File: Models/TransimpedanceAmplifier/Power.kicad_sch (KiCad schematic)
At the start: 0 parts

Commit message: Add tolerancing to the TIA regulator voltages
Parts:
- added U10: LM79L15, -15V, 5%, LP3_TEX, symbol LM79L:LM79L05ACZ_LFT1
- added U7: LM78L05, 5V, 5%, LP3_TEX, symbol LM78L:LM78L05ACZ_LFT1
- added U8: LM78L15, 15V, 5%, LP3_TEX, symbol LM78L:LM78L05ACZ_LFT1
- added U9: LM79L05, -5V, 5%, LP3_TEX, symbol LM79L:LM79L05ACZ_LFT1

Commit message: Save progress
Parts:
- removed U10: LM79L15, -15V, 5%, LP3_TEX, symbol LM79L:LM79L05ACZ_LFT1
- removed U7: LM78L05, 5V, 5%, LP3_TEX, symbol LM78L:LM78L05ACZ_LFT1
- removed U8: LM78L15, 15V, 5%, LP3_TEX, symbol LM78L:LM78L05ACZ_LFT1
- removed U9: LM79L05, -5V, 5%, LP3_TEX, symbol LM79L:LM79L05ACZ_LFT1
- added BT1, BT2, BT3, BT4, BT5, BT6: 9V, symbol Device:Battery
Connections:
- new net: BT4.2 (-), BT5.1 (+)
- new net: BT5.2 (-), BT6.1 (+)
- new net: BT1.2 (-), BT2.1 (+)
- new net: BT2.2 (-), BT3.1 (+)
- new net -27V: BT6.2 (-)
- new net 27V: BT1.1 (+)
- new net GND: BT3.2 (-), BT4.1 (+)
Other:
- added sheet Converter_LowVoltage (Converter_LowVoltage.kicad_sch)
- added sheet HighVoltage (HighVoltage.kicad_sch)
- added sheet PreAmp_LowVoltage (PreAmp_LowVoltage.kicad_sch)
- note added: "Negative power supply Guaranteed below -17.5 V for 0.3 A-hours"
- note added: "Positive power supply Guaranteed above 17.5 V for 0.3 A-hours 20 mA load condition ~26.9 V @ 0.0 hours ~17.5 V @ 15.0 hours 100 mA load condition ~26.6 V @ 0.0 hours ~17.5 V @ 3.0 hours"

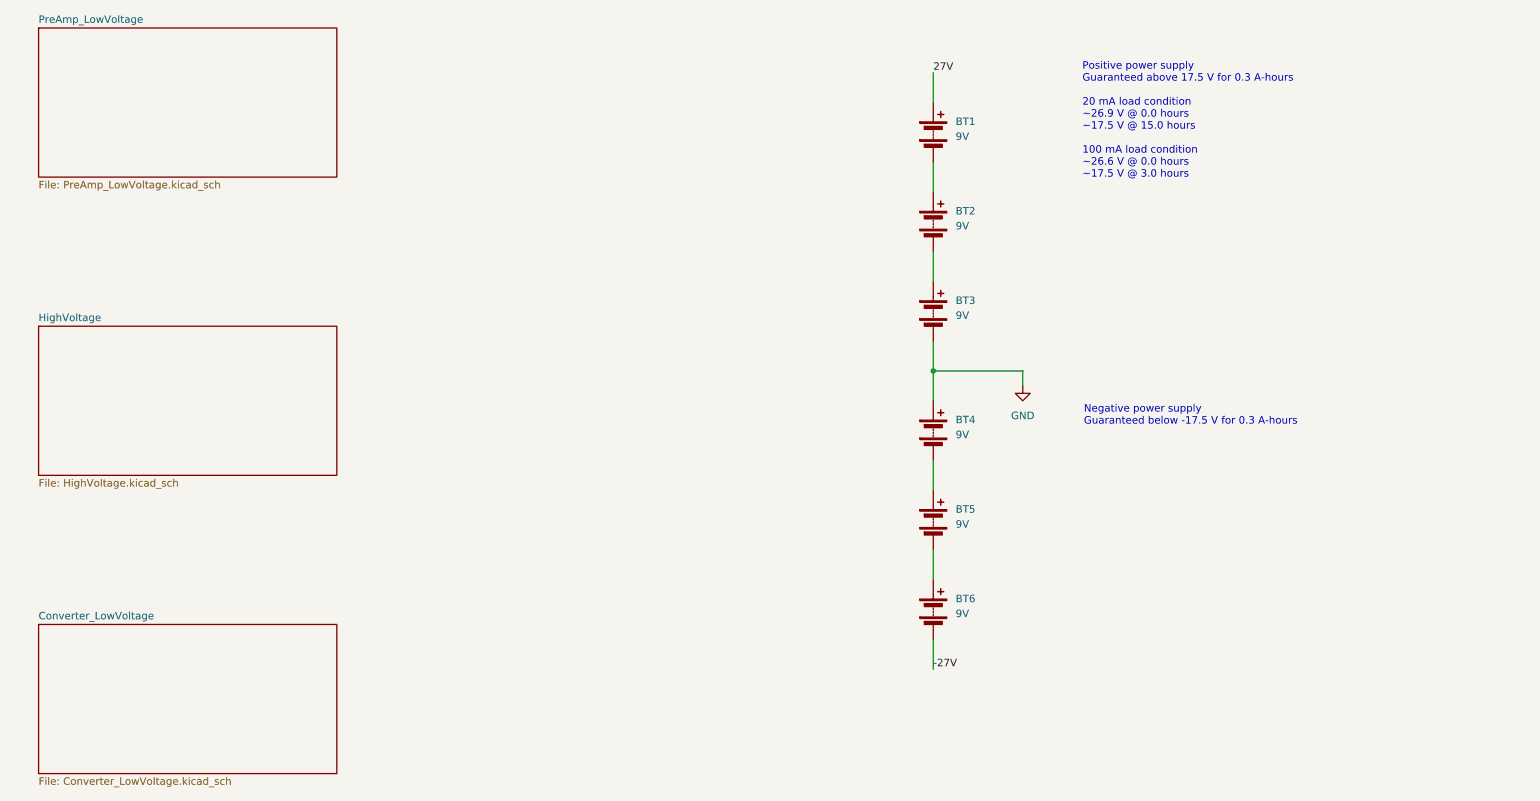
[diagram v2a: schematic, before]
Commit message: Added the 3.3V regulator choice
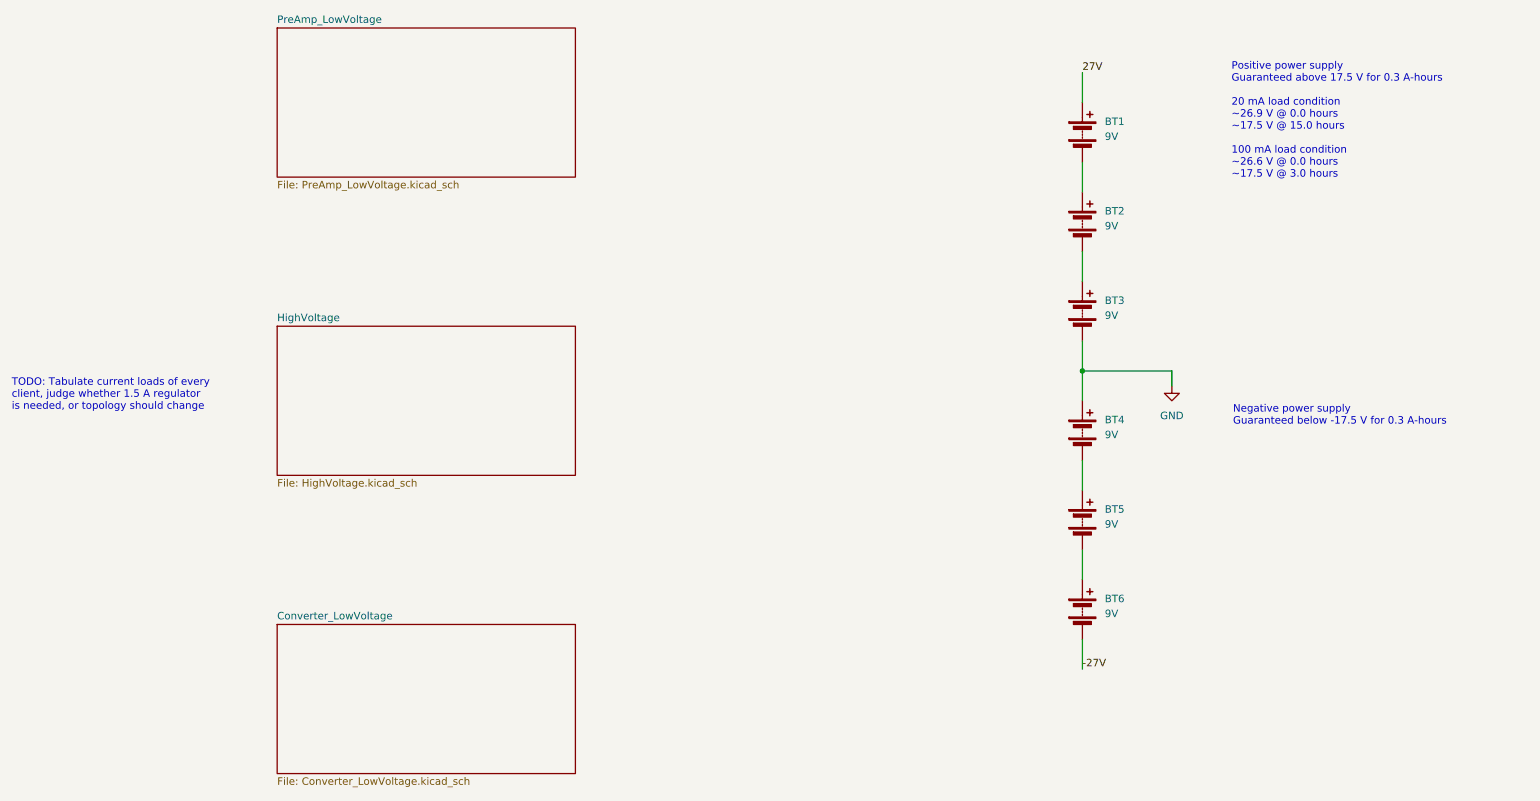
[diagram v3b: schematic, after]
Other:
- note added: "TODO: Tabulate current loads of every client, judge whether 1.5 A regulator is needed, or topology should change"
- moved on the sheet: BT1, BT2, BT3, BT4, BT5, BT6

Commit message: Labeled all the input/output nodes of the power subsystems
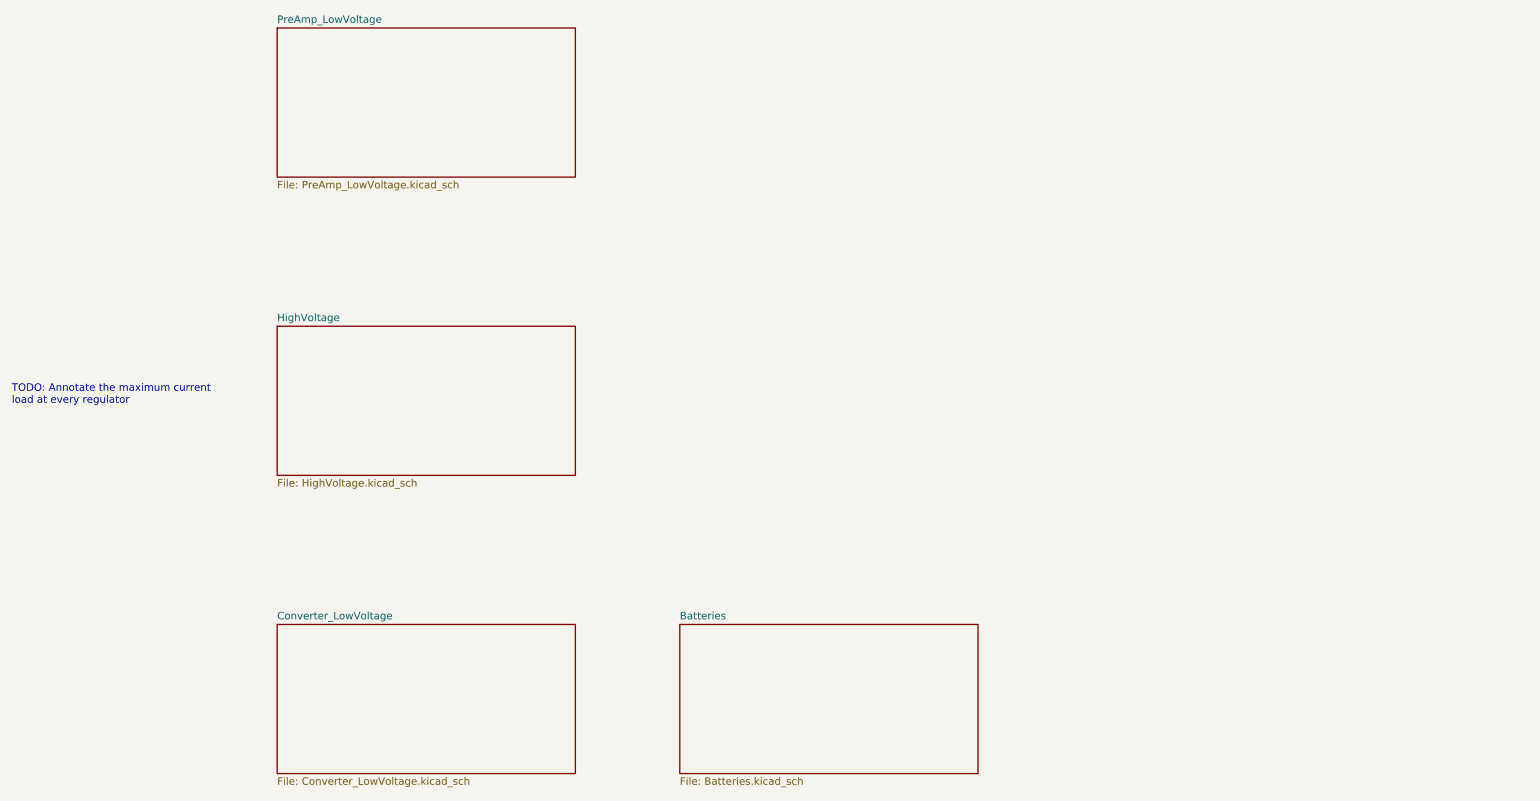
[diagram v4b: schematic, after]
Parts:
- removed BT1, BT2, BT3, BT4, BT5, BT6: 9V, symbol Device:Battery
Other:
- added sheet Batteries (Batteries.kicad_sch)
- note added: "TODO: Annotate the maximum current load at every regulator"
- note removed: "Negative power supply Guaranteed below -17.5 V for 0.3 A-hours"
- note removed: "Positive power supply Guaranteed above 17.5 V for 0.3 A-hours 20 mA load condition ~26.9 V @ 0.0 hours ~17.5 V @ 15.0 hours 100 mA load condition ~26.6 V @ 0.0 hours ~17.5 V @ 3.0 hours"
- note removed: "TODO: Tabulate current loads of every client, judge whether 1.5 A regulator is needed, or topology should change"

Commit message: Resolved the unknown regarding too much current into the 100 mA regulator
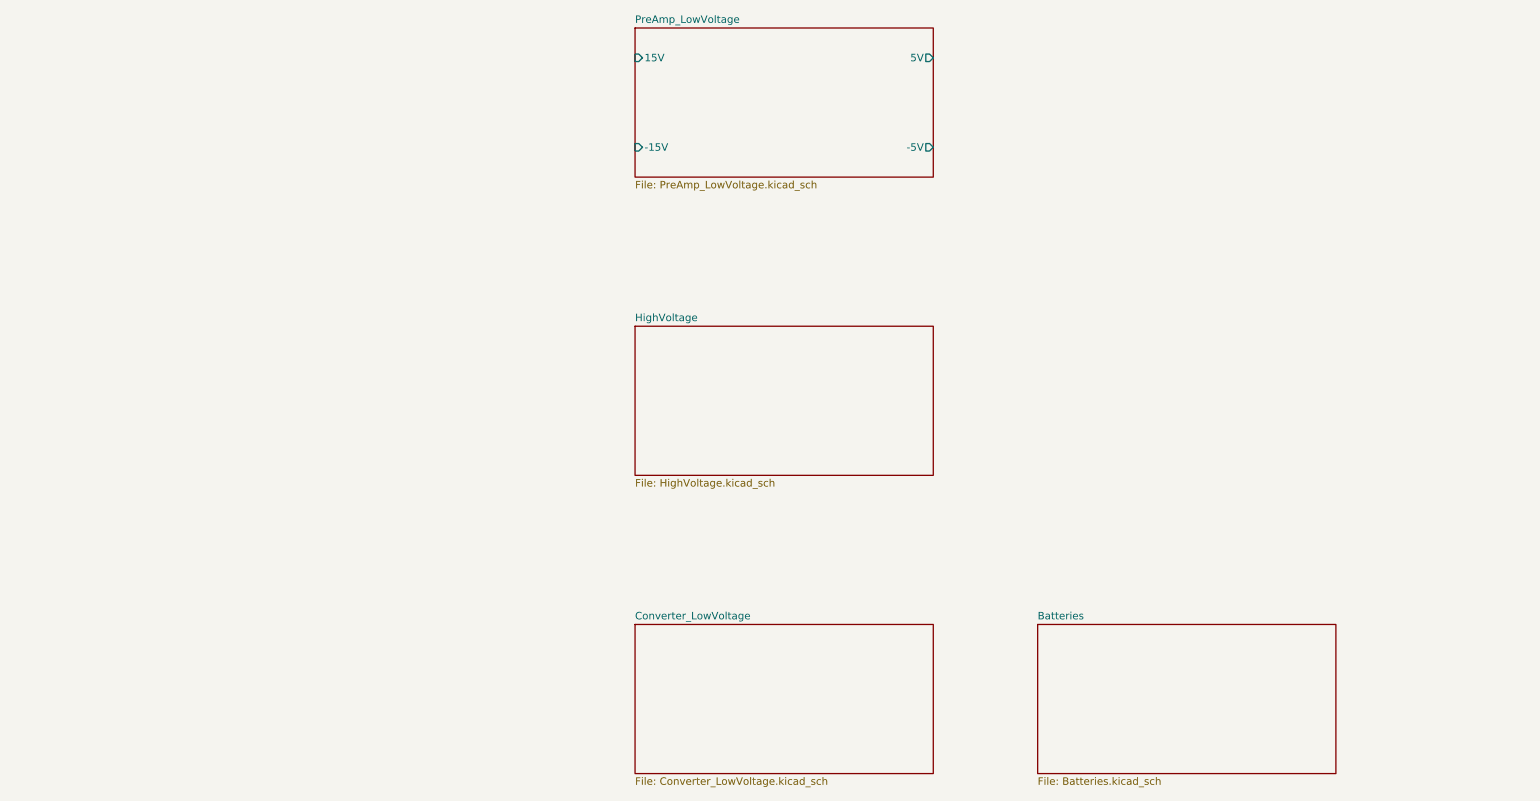
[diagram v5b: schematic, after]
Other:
- sheet PreAmp_LowVoltage ports: added -15V, -5V, 15V, 5V; removed none
- note removed: "TODO: Annotate the maximum current load at every regulator"
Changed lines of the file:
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@@
 	(generator_version "9.0")
 	(paper "A4")
-	(text "TODO: Annotate the maximum current\nload at every regulator"
-		(exclude_from_sim no)
-		(at 20.828 87.884 0)
-		(effects
-			(font
-				(size 1.27 1.27)
-			)
-			(justify left)
-		)
-	)
 	(sheet
-		(at 66.04 25.4)
+		(at 127 25.4)
 		(size 50.8 25.4)
 		(exclude_from_sim no)
@@
 		)
 		(property "Sheetname" "PreAmp_LowVoltage"
-			(at 66.04 24.6884 0)
+			(at 127 24.6884 0)
 			(effects
 				(font
@@
 		)
 		(property "Sheetfile" "PreAmp_LowVoltage.kicad_sch"
-			(at 66.04 51.3846 0)
+			(at 127 51.3846 0)
 			(effects
 				(font
@@
 				)
 				(justify left top)
+			)
+		)
+		(pin "-5V" output
+			(at 177.8 45.72 0)
+			(effects
+				(font
+					(size 1.27 1.27)
+				)
+				(justify right)
+			)
+		)
+		(pin "-15V" input
+			(at 127 45.72 180)
+			(effects
+				(font
+					(size 1.27 1.27)
+				)
+				(justify left)
+			)
+		)
+		(pin "5V" output
+			(at 177.8 30.48 0)
+			(effects
+				(font
+					(size 1.27 1.27)
+				)
+				(justify right)
+			)
+		)
+		(pin "15V" input
+			(at 127 30.48 180)
+			(effects
+				(font
+					(size 1.27 1.27)
+				)
+				(justify left)
 			)
 		)
@@
 	)
 	(sheet
-		(at 66.04 127)
+		(at 127 127)
 		(size 50.8 25.4)
 		(exclude_from_sim no)
@@
 		)
 		(property "Sheetname" "Converter_LowVoltage"
-			(at 66.04 126.2884 0)
+			(at 127 126.2884 0)
 			(effects
 				(font
@@
 		)
 		(property "Sheetfile" "Converter_LowVoltage.kicad_sch"
-			(at 66.04 152.9846 0)
+			(at 127 152.9846 0)
 			(effects
 				(font
@@
 	)
 	(sheet
-		(at 66.04 76.2)
+		(at 127 76.2)
 		(size 50.8 25.4)
 		(exclude_from_sim no)
@@
 		)
 		(property "Sheetname" "HighVoltage"
-			(at 66.04 75.4884 0)
+			(at 127 75.4884 0)
 			(effects
 				(font
@@
 		)
 		(property "Sheetfile" "HighVoltage.kicad_sch"
-			(at 66.04 102.1846 0)
+			(at 127 102.1846 0)
 			(effects
 				(font
@@
 	)
 	(sheet
-		(at 134.62 127)
+		(at 195.58 127)
 		(size 50.8 25.4)
 		(exclude_from_sim no)
@@
 		)
 		(property "Sheetname" "Batteries"
-			(at 134.62 126.2884 0)
+			(at 195.58 126.2884 0)
 			(effects
 				(font
@@
 		)
 		(property "Sheetfile" "Batteries.kicad_sch"
-			(at 134.62 152.9846 0)
+			(at 195.58 152.9846 0)
 			(effects
 				(font

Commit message: Finished connecting the subsystems of the power module
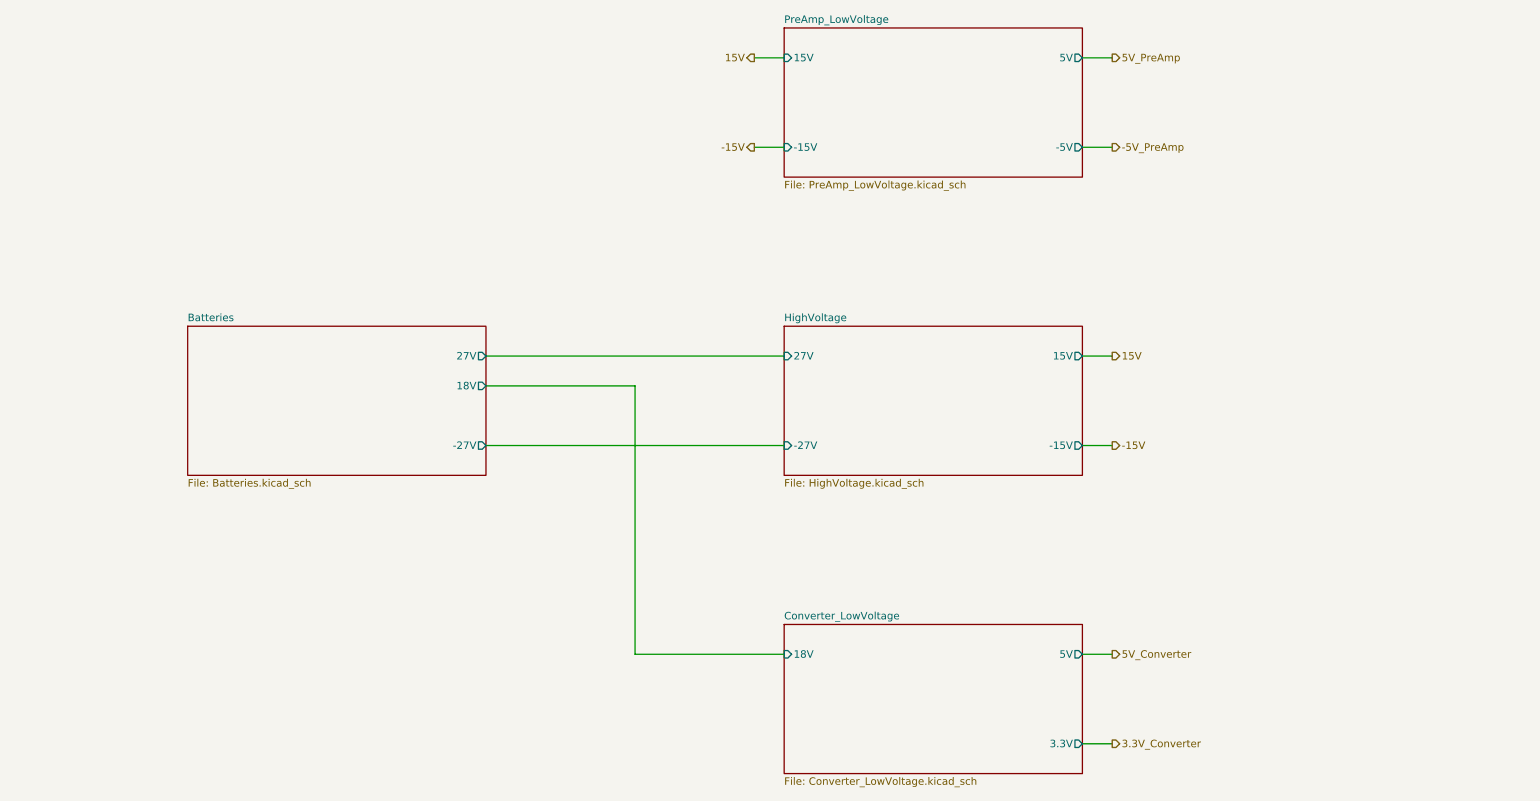
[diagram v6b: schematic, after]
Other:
- sheet Batteries ports: added -27V, 18V, 27V; removed none
- sheet Converter_LowVoltage ports: added 18V, 3.3V, 5V; removed none
- sheet HighVoltage ports: added -15V, -27V, 15V, 27V; removed none

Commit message: Save progress
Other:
- note added: "TODO: Tabulate the maximum expected current at each regulator, to see whether LM78xx is needed anywhere instead of LM78Lxx"
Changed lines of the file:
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@@
 	(generator_version "9.0")
 	(paper "A4")
+	(text "TODO: Tabulate the maximum expected\ncurrent at each regulator, to see\nwhether LM78xx is needed anywhere\ninstead of LM78Lxx"
+		(exclude_from_sim no)
+		(at 51.562 30.226 0)
+		(effects
+			(font
+				(size 1.27 1.27)
+			)
+			(justify left)
+		)
+	)
 	(wire
 		(pts

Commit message: Save progress after a major refactoring
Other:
- removed sheet Converter_LowVoltage
- removed sheet PreAmp_LowVoltage
- added sheet LowVoltage_Converter (LowVoltage_Converter.kicad_sch)
- added sheet LowVoltage_PreAmp (LowVoltage_PreAmp.kicad_sch)
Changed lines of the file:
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@@
-	)
-	(sheet
-		(at 152.4 25.4)
-		(size 50.8 25.4)
-		(exclude_from_sim no)
-		(in_bom yes)
-		(on_board yes)
-		(dnp no)
-		(fields_autoplaced yes)
-		(stroke
-			(width 0.1524)
-			(type solid)
-		)
-		(fill
-			(color 0 0 0 0.0000)
-		)
-		(property "Sheetname" "PreAmp_LowVoltage"
-			(at 152.4 24.6884 0)
-			(effects
-				(font
-					(size 1.27 1.27)
-				)
-				(justify left bottom)
-			)
-		)
-		(property "Sheetfile" "PreAmp_LowVoltage.kicad_sch"
-			(at 152.4 51.3846 0)
-			(effects
-				(font
-					(size 1.27 1.27)
-				)
-				(justify left top)
-			)
-		)
-		(pin "-5V" output
-			(at 203.2 45.72 0)
-			(effects
-				(font
-					(size 1.27 1.27)
-				)
-				(justify right)
-			)
-		)
-		(pin "-15V" input
-			(at 152.4 45.72 180)
-			(effects
-				(font
-					(size 1.27 1.27)
-				)
-				(justify left)
-			)
-		)
-		(pin "5V" output
-			(at 203.2 30.48 0)
-			(effects
-				(font
-					(size 1.27 1.27)
-				)
-				(justify right)
-			)
-		)
-		(pin "15V" input
-			(at 152.4 30.48 180)
-			(effects
-				(font
-					(size 1.27 1.27)
-				)
-				(justify left)
-			)
-		)
-		(instances
-			(project "TransimpedanceAmplifier"
-				(path "/ec9f2ae3-e40d-40eb-9760-2b611ee8efd1/68e8bf39-bd36-49ed-a85c-9ce753018063"
-					(page "11")
-				)
-			)
-		)
-	)
-	(sheet
-		(at 152.4 127)
-		(size 50.8 25.4)
-		(exclude_from_sim no)
-		(in_bom yes)
-		(on_board yes)
-		(dnp no)
-		(fields_autoplaced yes)
-		(stroke
-			(width 0.1524)
-			(type solid)
-		)
-		(fill
-			(color 0 0 0 0.0000)
-		)
-		(property "Sheetname" "Converter_LowVoltage"
-			(at 152.4 126.2884 0)
-			(effects
-				(font
-					(size 1.27 1.27)
-				)
-				(justify left bottom)
-			)
-		)
-		(property "Sheetfile" "Converter_LowVoltage.kicad_sch"
-			(at 152.4 152.9846 0)
-			(effects
-				(font
-					(size 1.27 1.27)
-				)
-				(justify left top)
-			)
-		)
-		(pin "3.3V" output
-			(at 203.2 147.32 0)
-			(effects
-				(font
-					(size 1.27 1.27)
-				)
-				(justify right)
-			)
-		)
-		(pin "5V" output
-			(at 203.2 132.08 0)
-			(effects
-				(font
-					(size 1.27 1.27)
-				)
-				(justify right)
-			)
-		)
-		(pin "18V" input
-			(at 152.4 132.08 180)
-			(effects
-				(font
-					(size 1.27 1.27)
-				)
-				(justify left)
-			)
-		)
-		(instances
-			(project "TransimpedanceAmplifier"
-				(path "/ec9f2ae3-e40d-40eb-9760-2b611ee8efd1/68e8bf39-bd36-49ed-a85c-9ce753018063"
-					(page "13")
-				)
-			)
-		)
 	)
 	(sheet
@@
 	)
 	(sheet
+		(at 152.4 127)
+		(size 50.8 25.4)
+		(exclude_from_sim no)
+		(in_bom yes)
+		(on_board yes)
+		(dnp no)
+		(fields_autoplaced yes)
+		(stroke
+			(width 0.1524)
+			(type solid)
+		)
+		(fill
+			(color 0 0 0 0.0000)
+		)
+		(property "Sheetname" "LowVoltage_Converter"
+			(at 152.4 126.2884 0)
+			(effects
+				(font
+					(size 1.27 1.27)
+				)
+				(justify left bottom)
+			)
+		)
+		(property "Sheetfile" "LowVoltage_Converter.kicad_sch"
+			(at 152.4 152.9846 0)
+			(effects
+				(font
+					(size 1.27 1.27)
+				)
+				(justify left top)
+			)
+		)
+		(instances
+			(project "TransimpedanceAmplifier"
+				(path "/ec9f2ae3-e40d-40eb-9760-2b611ee8efd1/68e8bf39-bd36-49ed-a85c-9ce753018063"
+					(page "16")
+				)
+			)
+		)
+	)
+	(sheet
 		(at 50.8 76.2)
 		(size 50.8 25.4)
@@
 				)
 			)
+		)
+	)
+	(sheet
+		(at 152.4 25.4)
+		(size 50.8 25.4)
+		(exclude_from_sim no)
+		(in_bom yes)
+		(on_board yes)
+		(dnp no)
+		(fields_autoplaced yes)
+		(stroke
+			(width 0.1524)
+			(type solid)
+		)
+		(fill
+			(color 0 0 0 0.0000)
+		)
+		(property "Sheetname" "LowVoltage_PreAmp"
+			(at 152.4 24.6884 0)
+			(effects
+				(font
+					(size 1.27 1.27)
+				)
+				(justify left bottom)
+			)
+		)
+		(property "Sheetfile" "LowVoltage_PreAmp.kicad_sch"
+			(at 152.4 51.3846 0)
+			(effects
+				(font
+					(size 1.27 1.27)
+				)
+				(justify left top)
+			)
+		)
+		(instances
+			(project "TransimpedanceAmplifier"
+				(path "/ec9f2ae3-e40d-40eb-9760-2b611ee8efd1/68e8bf39-bd36-49ed-a85c-9ce753018063"
+					(page "15")
+				)
+			)
